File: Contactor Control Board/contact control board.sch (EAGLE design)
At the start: 23 parts, among them Q4 MOSFET-NCHANNELFQP30N06L

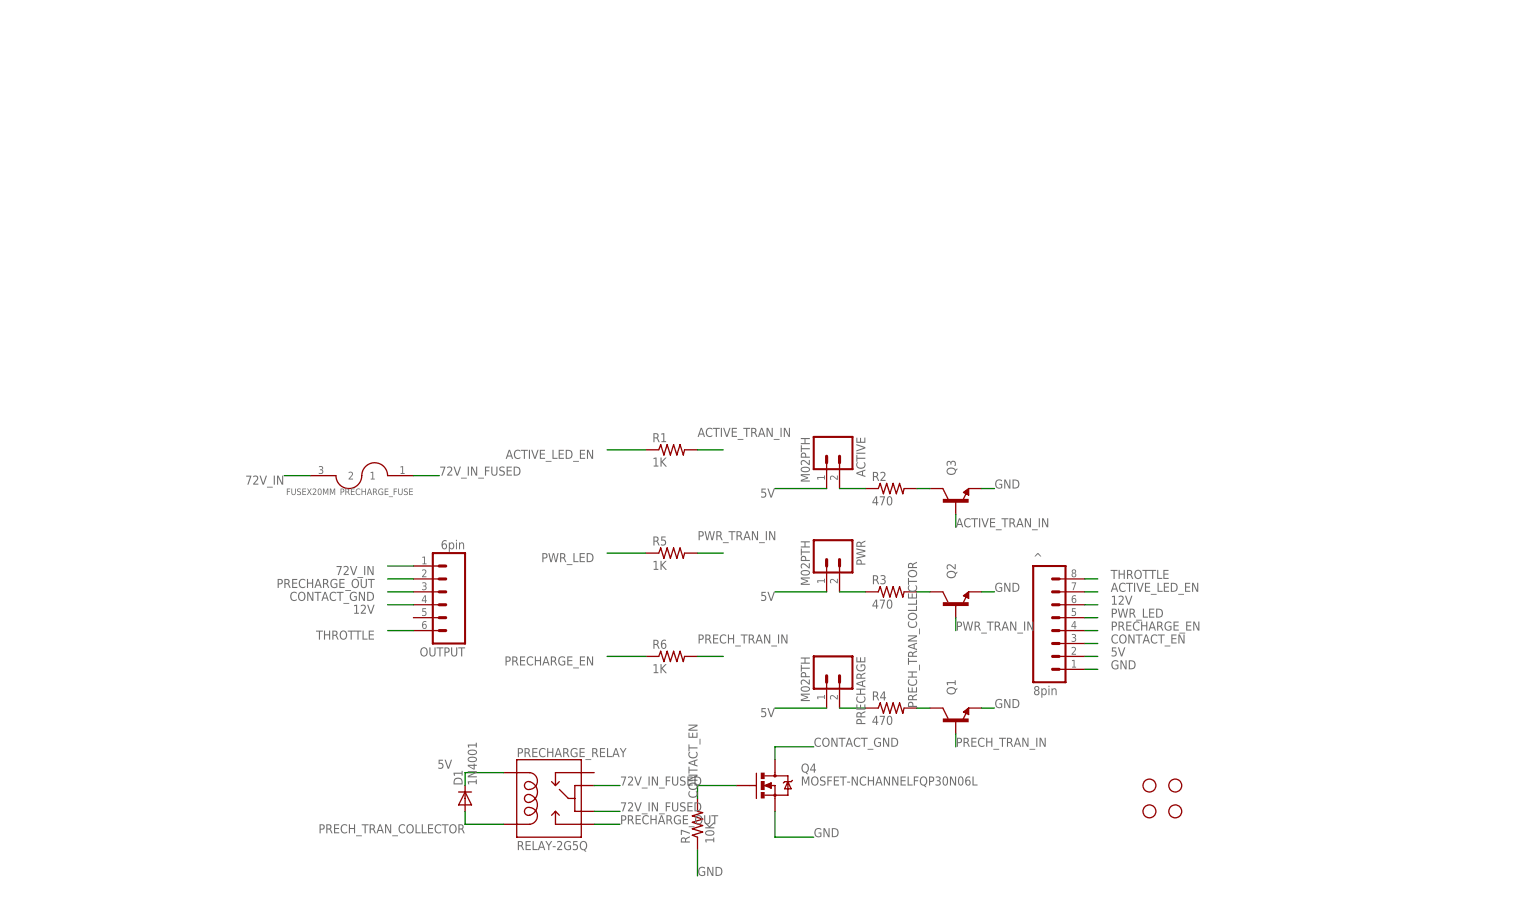
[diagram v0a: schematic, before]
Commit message: Adding capacitor charge state sense for CCB
Theoretical part selection. Not for usage until testing!
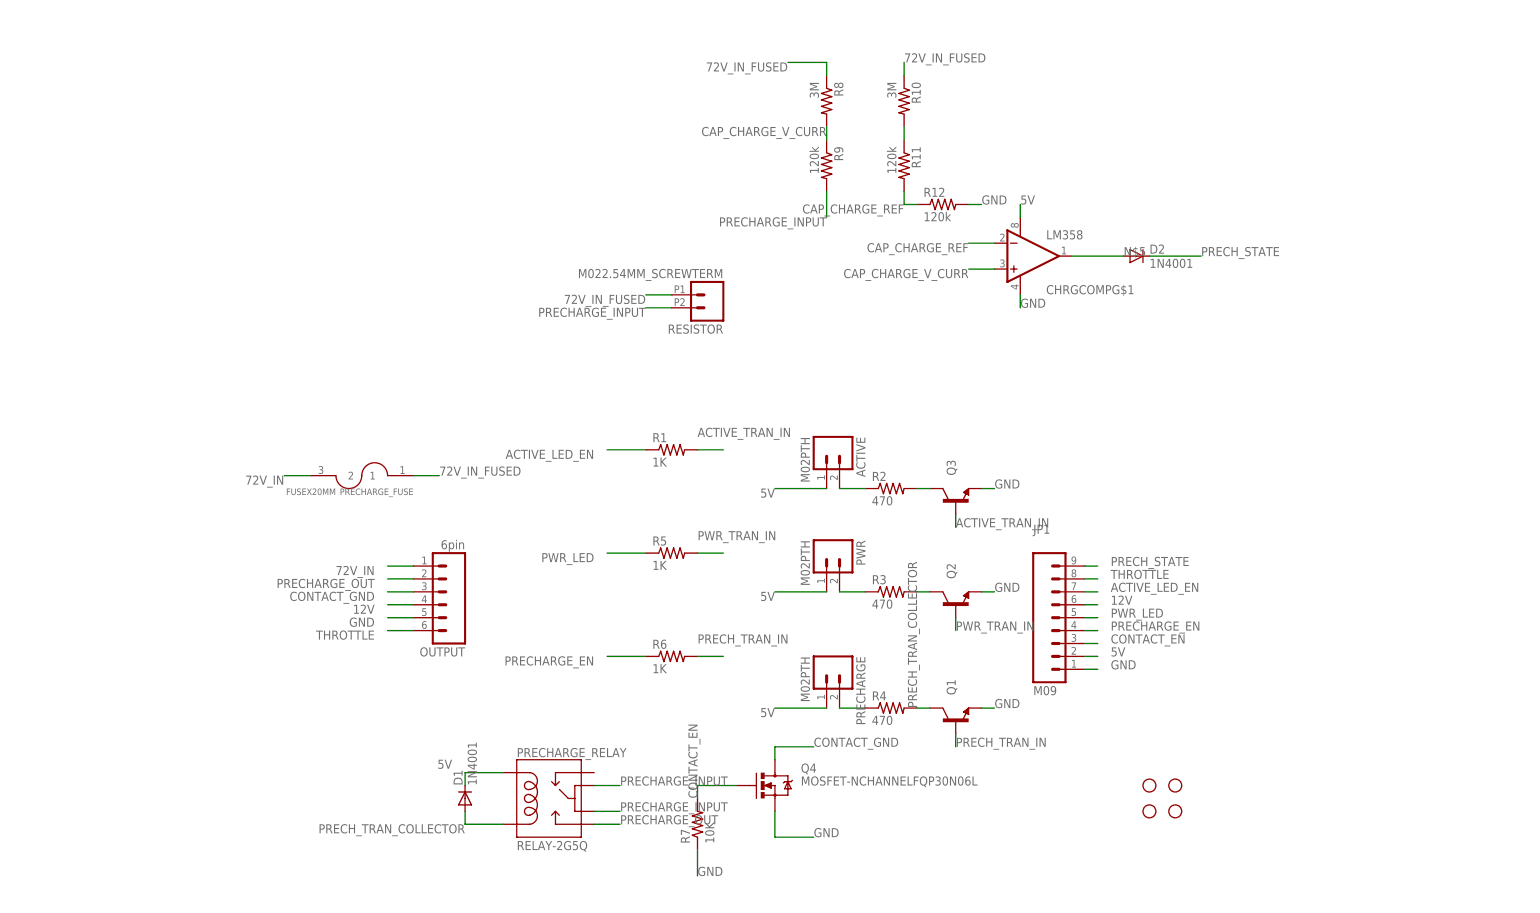
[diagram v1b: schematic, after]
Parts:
- removed ^: 8pin, SparkFun-Connectors:M081X08
- added CHRGCOMP: LM358, SparkFun-AnalogIC:LM358
- added D2: 1N4001, SparkFun-DiscreteSemi:DIODEPTH
- added JP1: M09, SparkFun-Connectors:M09
- added R10, R8: 3M, SparkFun-Resistors:RESISTORPTH-1/4W
- added R11, R12, R9: 120k, SparkFun-Resistors:RESISTORPTH-1/4W
- added RESISTOR: M022.54MM_SCREWTERM, SparkFun-Connectors:M022.54MM_SCREWTERM
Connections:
- new net CAP_CHARGE_REF: CHRGCOMPG$1.-IN, R11.2, R12.1
- new net CAP_CHARGE_V_CURR: CHRGCOMPG$1.+IN, R8.2, R9.1
- new net N$3: R10.2, R11.1
- new net N$5: CHRGCOMPG$1.OUT, D2.A
- new net PRECHARGE_INPUT: PRECHARGE_RELAY.5, PRECHARGE_RELAY.6, R9.2, RESISTOR.2
- new net PRECH_STATE: D2.C, JP1.9
- net 12V: now also JP1.6; no longer ^.6
- net 5V: now also CHRGCOMPG$1.V+, JP1.2; no longer ^.2
- net 72V_IN_FUSED: now also R10.1, R8.1, RESISTOR.1; no longer PRECHARGE_RELAY.5, PRECHARGE_RELAY.6
- net ACTIVE_LED_EN: now also JP1.7; no longer ^.7
- net CONTACT_EN: now also JP1.3; no longer ^.3
- net GND: now also CHRGCOMPG$1.V-, JP1.1, OUTPUT.5, R12.2; no longer ^.1
- net PRECHARGE_EN: now also JP1.4; no longer ^.4
- net PWR_LED: now also JP1.5; no longer ^.5
- net THROTTLE: now also JP1.8; no longer ^.8

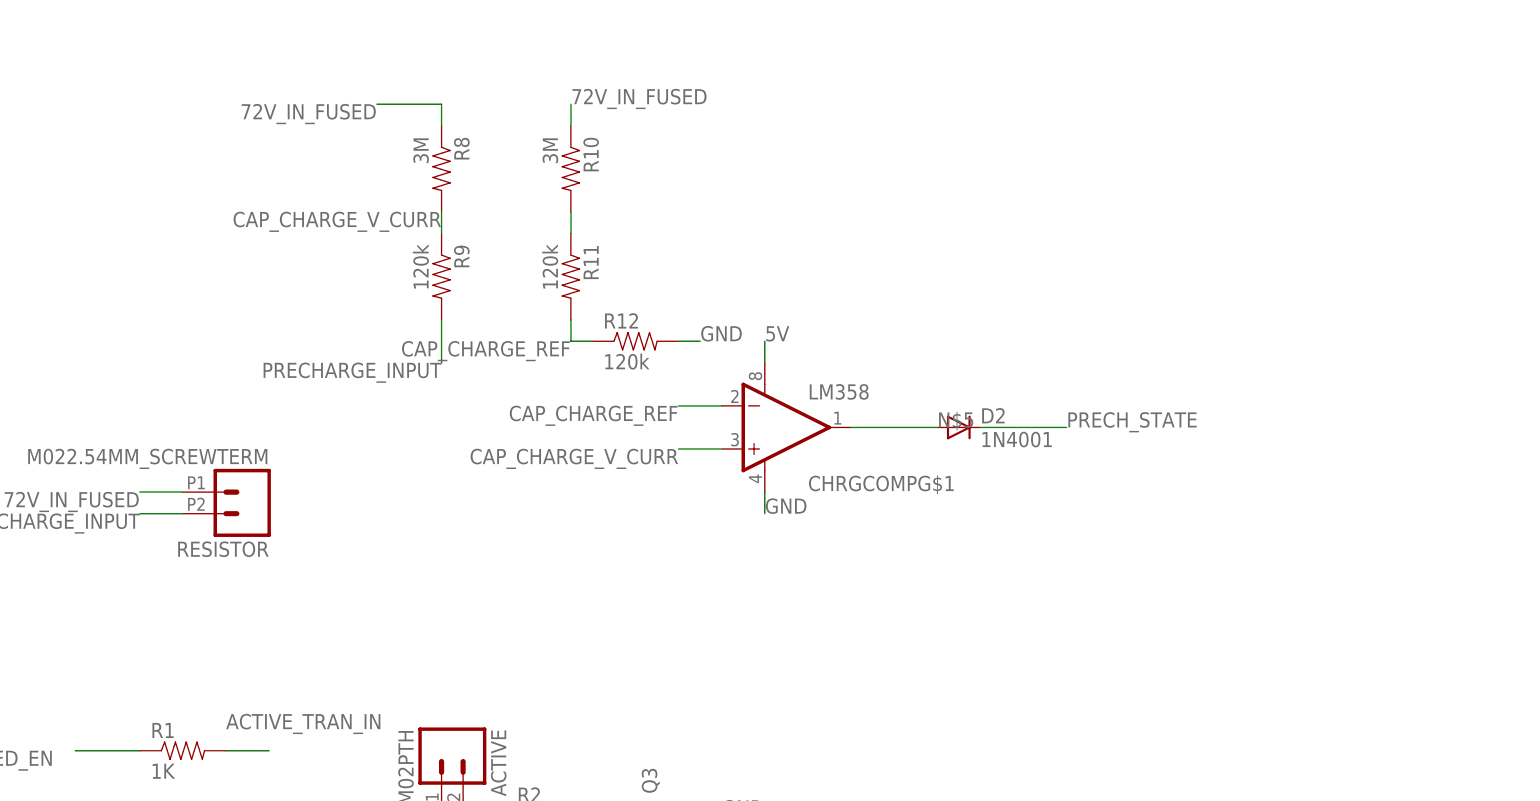
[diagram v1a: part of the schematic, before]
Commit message: Added inverter w/ schmitt trigger to the output of the opamp to fixup its outputs.
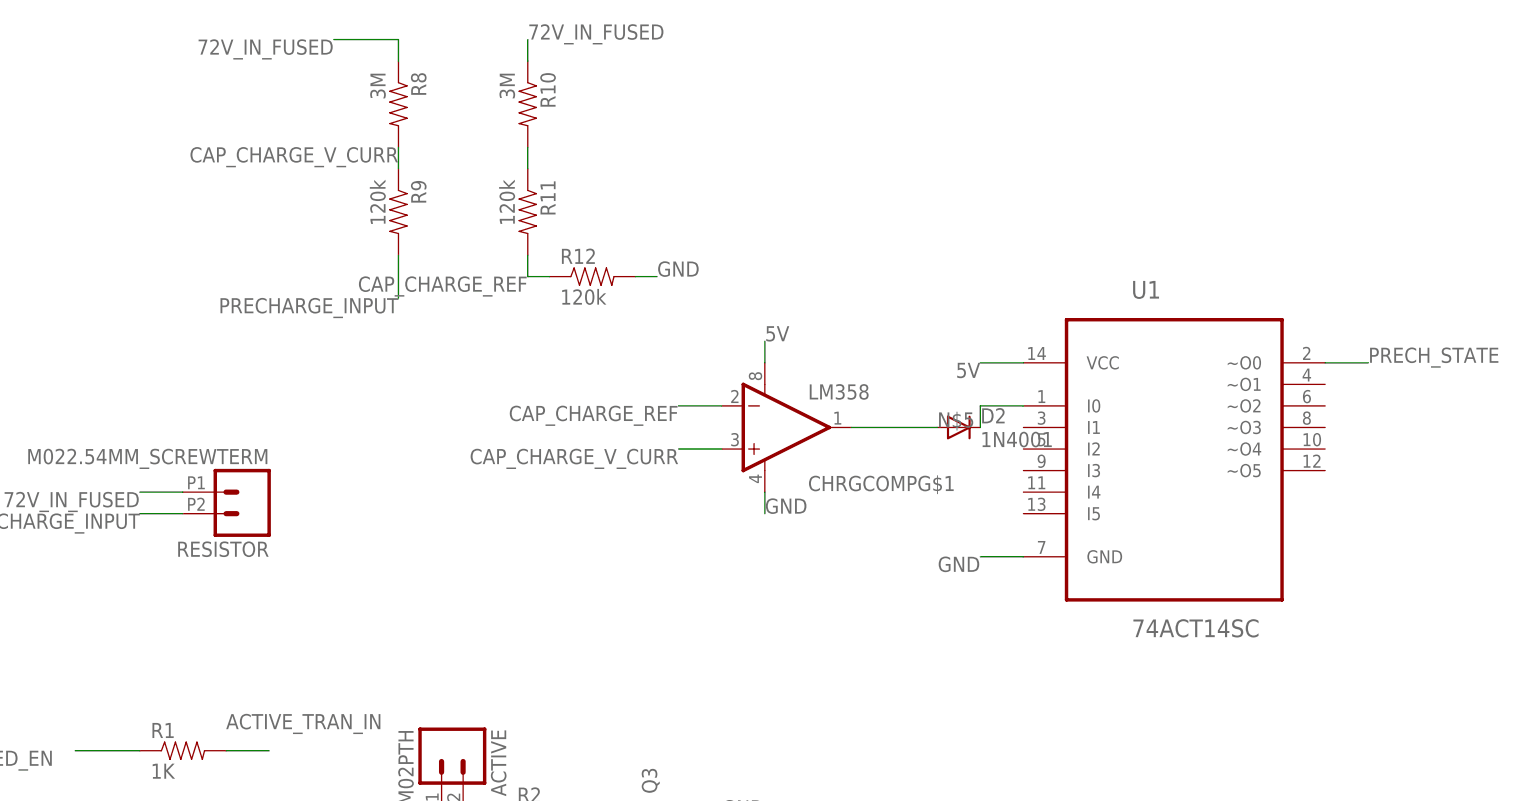
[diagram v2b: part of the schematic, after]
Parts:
- added U1: 74ACT14SC, Fairchild_By_element14_Batch_1:74ACT14SC
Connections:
- new net N$6: U1.I0
- net 5V: now also U1.VCC
- net GND: now also U1.GND
- net PRECH_STATE: now also U1.~O0; no longer D2.C
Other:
- moved on the sheet: R10, R11, R12, R8, R9
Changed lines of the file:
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@@
 <part name="R11" library="SparkFun-Resistors" deviceset="RESISTOR" device="PTH-1/4W" value="120k"/>
 <part name="R12" library="SparkFun-Resistors" deviceset="RESISTOR" device="PTH-1/4W" value="120k"/>
+<part name="U1" library="Fairchild_By_element14_Batch_1" deviceset="74ACT14SC" device=""/>
 </parts>
 <sheets>
@@
 <instance part="CHRGCOMP" gate="G$1" x="114.3" y="121.92"/>
 <instance part="D2" gate="G$1" x="137.16" y="121.92"/>
-<instance part="R8" gate="G$1" x="76.2" y="152.4" rot="R270"/>
-<instance part="R9" gate="G$1" x="76.2" y="139.7" rot="R270"/>
-<instance part="R10" gate="G$1" x="91.44" y="152.4" rot="R270"/>
-<instance part="R11" gate="G$1" x="91.44" y="139.7" rot="R270"/>
-<instance part="R12" gate="G$1" x="99.06" y="132.08"/>
+<instance part="R8" gate="G$1" x="71.12" y="160.02" rot="R270"/>
+<instance part="R9" gate="G$1" x="71.12" y="147.32" rot="R270"/>
+<instance part="R10" gate="G$1" x="86.36" y="160.02" rot="R270"/>
+<instance part="R11" gate="G$1" x="86.36" y="147.32" rot="R270"/>
+<instance part="R12" gate="G$1" x="93.98" y="139.7"/>
+<instance part="U1" gate="A" x="162.56" y="121.92"/>
 </instances>
 <busses>
@@
 <label x="114.3" y="132.08" size="1.778" layer="95"/>
 </segment>
+<segment>
+<pinref part="U1" gate="A" pin="VCC"/>
+<wire x1="144.78" y1="129.54" x2="139.7" y2="129.54" width="0.2032" layer="91"/>
+<label x="139.7" y="129.54" size="1.778" layer="95" rot="R180"/>
+</segment>
 </net>
 <net name="GND" class="0">
@@
 <segment>
 <pinref part="R12" gate="G$1" pin="2"/>
-<wire x1="104.14" y1="132.08" x2="106.68" y2="132.08" width="0.2032" layer="91"/>
-<label x="106.68" y="132.08" size="1.778" layer="95"/>
+<wire x1="99.06" y1="139.7" x2="101.6" y2="139.7" width="0.2032" layer="91"/>
+<label x="101.6" y="139.7" size="1.778" layer="95"/>
+</segment>
+<segment>
+<pinref part="U1" gate="A" pin="GND"/>
+<wire x1="144.78" y1="106.68" x2="139.7" y2="106.68" width="0.2032" layer="91"/>
+<label x="139.7" y="106.68" size="1.778" layer="95" rot="R180"/>
 </segment>
 </net>
@@
 <segment>
 <pinref part="R10" gate="G$1" pin="1"/>
-<wire x1="91.44" y1="157.48" x2="91.44" y2="160.02" width="0.2032" layer="91"/>
-<label x="91.44" y="160.02" size="1.778" layer="95"/>
+<wire x1="86.36" y1="165.1" x2="86.36" y2="167.64" width="0.2032" layer="91"/>
+<label x="86.36" y="167.64" size="1.778" layer="95"/>
 </segment>
 <segment>
 <pinref part="R8" gate="G$1" pin="1"/>
-<wire x1="76.2" y1="157.48" x2="76.2" y2="160.02" width="0.2032" layer="91"/>
-<wire x1="76.2" y1="160.02" x2="68.58" y2="160.02" width="0.2032" layer="91"/>
-<label x="68.58" y="160.02" size="1.778" layer="95" rot="R180"/>
+<wire x1="71.12" y1="165.1" x2="71.12" y2="167.64" width="0.2032" layer="91"/>
+<wire x1="71.12" y1="167.64" x2="63.5" y2="167.64" width="0.2032" layer="91"/>
+<label x="63.5" y="167.64" size="1.778" layer="95" rot="R180"/>
 </segment>
 </net>
@@
 </segment>
 <segment>
-<pinref part="D2" gate="G$1" pin="C"/>
-<wire x1="139.7" y1="121.92" x2="149.86" y2="121.92" width="0.2032" layer="91"/>
-<label x="149.86" y="121.92" size="1.778" layer="95"/>
+<pinref part="U1" gate="A" pin="~O0"/>
+<wire x1="180.34" y1="129.54" x2="185.42" y2="129.54" width="0.2032" layer="91"/>
+<label x="185.42" y="129.54" size="1.778" layer="95"/>
 </segment>
 </net>
@@
 <segment>
 <pinref part="R9" gate="G$1" pin="2"/>
-<wire x1="76.2" y1="134.62" x2="76.2" y2="129.54" width="0.2032" layer="91"/>
-<label x="76.2" y="129.54" size="1.778" layer="95" rot="R180"/>
+<wire x1="71.12" y1="142.24" x2="71.12" y2="137.16" width="0.2032" layer="91"/>
+<label x="71.12" y="137.16" size="1.778" layer="95" rot="R180"/>
 </segment>
 </net>
@@
 <pinref part="R11" gate="G$1" pin="2"/>
 <pinref part="R12" gate="G$1" pin="1"/>
-<wire x1="91.44" y1="134.62" x2="91.44" y2="132.08" width="0.2032" layer="91"/>
-<wire x1="91.44" y1="132.08" x2="93.98" y2="132.08" width="0.2032" layer="91"/>
-<label x="91.44" y="132.08" size="1.778" layer="95" rot="R180"/>
+<wire x1="86.36" y1="142.24" x2="86.36" y2="139.7" width="0.2032" layer="91"/>
+<wire x1="86.36" y1="139.7" x2="88.9" y2="139.7" width="0.2032" layer="91"/>
+<label x="86.36" y="139.7" size="1.778" layer="95" rot="R180"/>
 </segment>
 </net>
@@
 <pinref part="R10" gate="G$1" pin="2"/>
 <pinref part="R11" gate="G$1" pin="1"/>
-<wire x1="91.44" y1="147.32" x2="91.44" y2="144.78" width="0.2032" layer="91"/>
+<wire x1="86.36" y1="154.94" x2="86.36" y2="152.4" width="0.2032" layer="91"/>
 </segment>
 </net>
@@
 <pinref part="R8" gate="G$1" pin="2"/>
 <pinref part="R9" gate="G$1" pin="1"/>
-<wire x1="76.2" y1="147.32" x2="76.2" y2="144.78" width="0.2032" layer="91"/>
-<label x="76.2" y="147.32" size="1.778" layer="95" rot="R180"/>
+<wire x1="71.12" y1="154.94" x2="71.12" y2="152.4" width="0.2032" layer="91"/>
+<label x="71.12" y="154.94" size="1.778" layer="95" rot="R180"/>
 </segment>
 <segment>
@@
 </segment>
 </net>
+<net name="N$6" class="0">
+<segment>
+<pinref part="U1" gate="A" pin="I0"/>
+<wire x1="144.78" y1="124.46" x2="139.7" y2="124.46" width="0.2032" layer="91"/>
+<wire x1="139.7" y1="121.92" x2="139.7" y2="124.46" width="0.2032" layer="91"/>
+</segment>
+</net>
